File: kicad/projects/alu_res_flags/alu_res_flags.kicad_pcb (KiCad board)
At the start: 2 copper layers, 203.2 x 97.8 mm, 61 parts, among them J1 RES_CRRYBRRW_EQ_IN, J2 Aux_connection, J3 Bus_connection, J4 Control_signal_backplane, J5 ECNZ_OUT, J6 LED_CONTROL, U1 74HC04, U10 74HC245, U11 74HC173, U12 74HC245, U2 74HC377, U3 74HC377, U4 74HC245, U5 74HC245, U6 74HC27, U7 74HC27, U8 74HC30, U9 74HC245

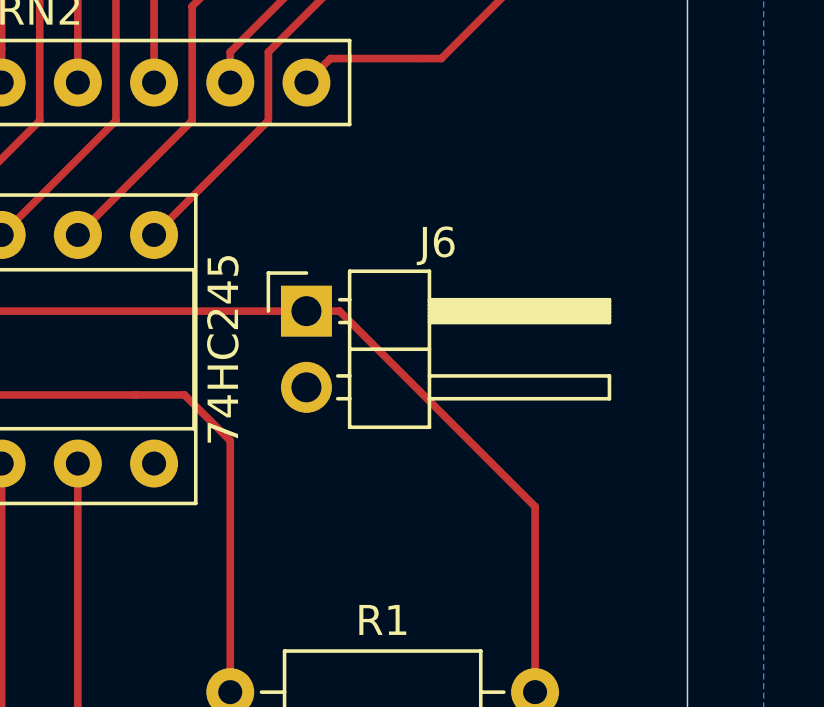
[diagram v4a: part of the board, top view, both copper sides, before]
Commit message: Add better labels to top power and LED control.
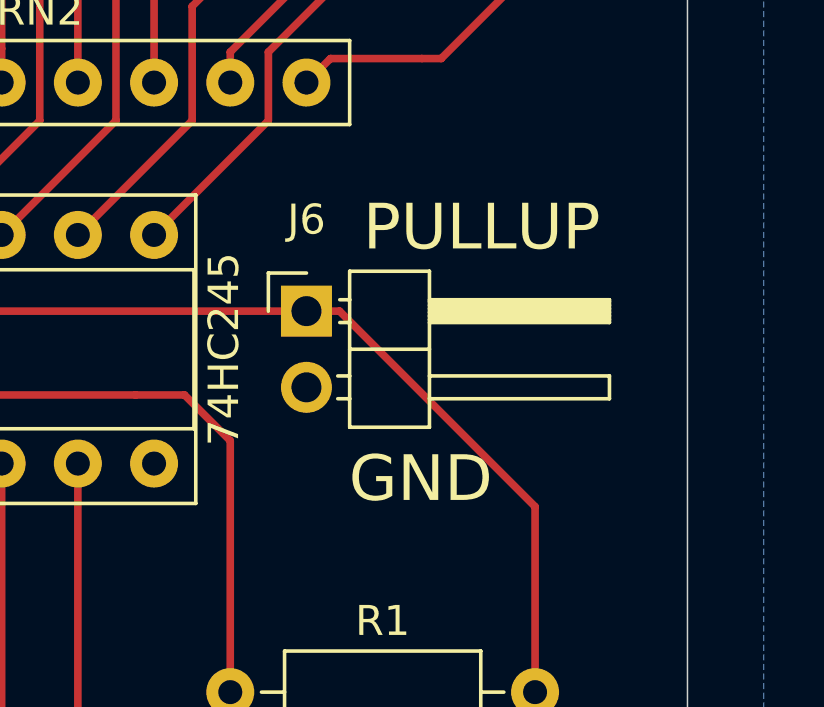
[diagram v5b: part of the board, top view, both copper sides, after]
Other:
- board text added: "GND"
- board text added: "PULLUP"
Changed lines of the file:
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@@
   (general
     (thickness 1.6)
-    (drawings 36)
+    (drawings 38)
     (tracks 1587)
     (zones 0)
@@
   )
   (setup
-    (last_trace_width 0.762)
+    (last_trace_width 0.254)
     (user_trace_width 0.762)
     (trace_clearance 0.2)
@@
     (descr "Through hole angled pin header, 1x02, 2.54mm pitch, 6mm pin length, single row")
     (tags "Through hole angled pin header THT 1x02 2.54mm single row")
-    (fp_text reference J6 (at 4.385 -2.27) (layer F.SilkS)
+    (fp_text reference J6 (at 0 -3.048) (layer F.SilkS)
       (effects (font (size 1 1) (thickness 0.15)))
     )
@@
     )
   )
+  (gr_text GND (at 245.11 89.408) (layer F.SilkS)
+    (effects (font (size 1.524 1.524) (thickness 0.254)))
+  )
+  (gr_text PULLUP (at 247.142 81.026) (layer F.SilkS)
+    (effects (font (size 1.524 1.524) (thickness 0.254)))
+  )
   (gr_arc (start 52.705 151.765) (end 50.8 151.765) (angle -90) (layer Edge.Cuts) (width 0.05))

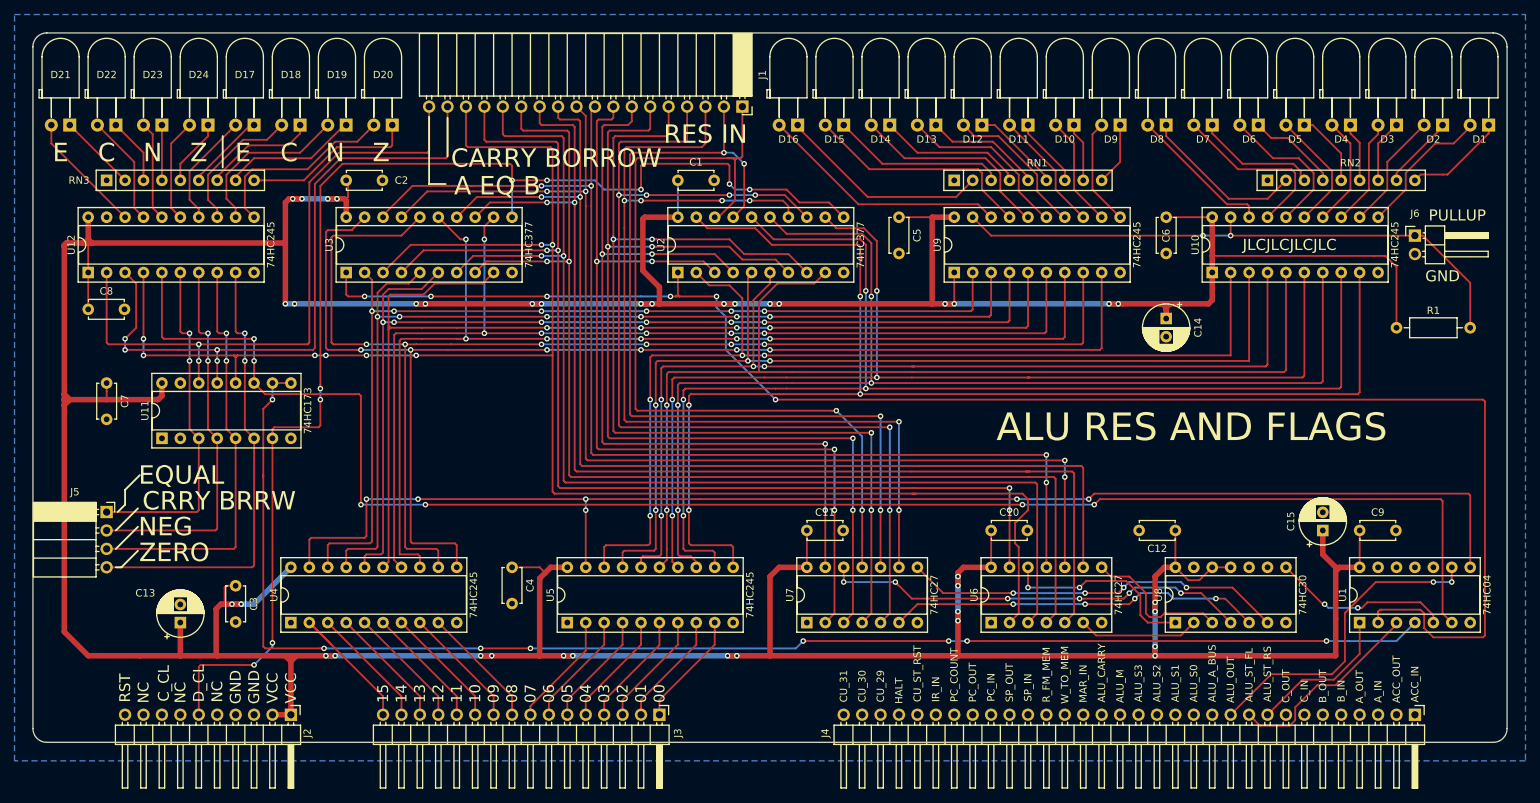
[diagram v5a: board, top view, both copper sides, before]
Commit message: Add pullups on bus output enable and update LED control.
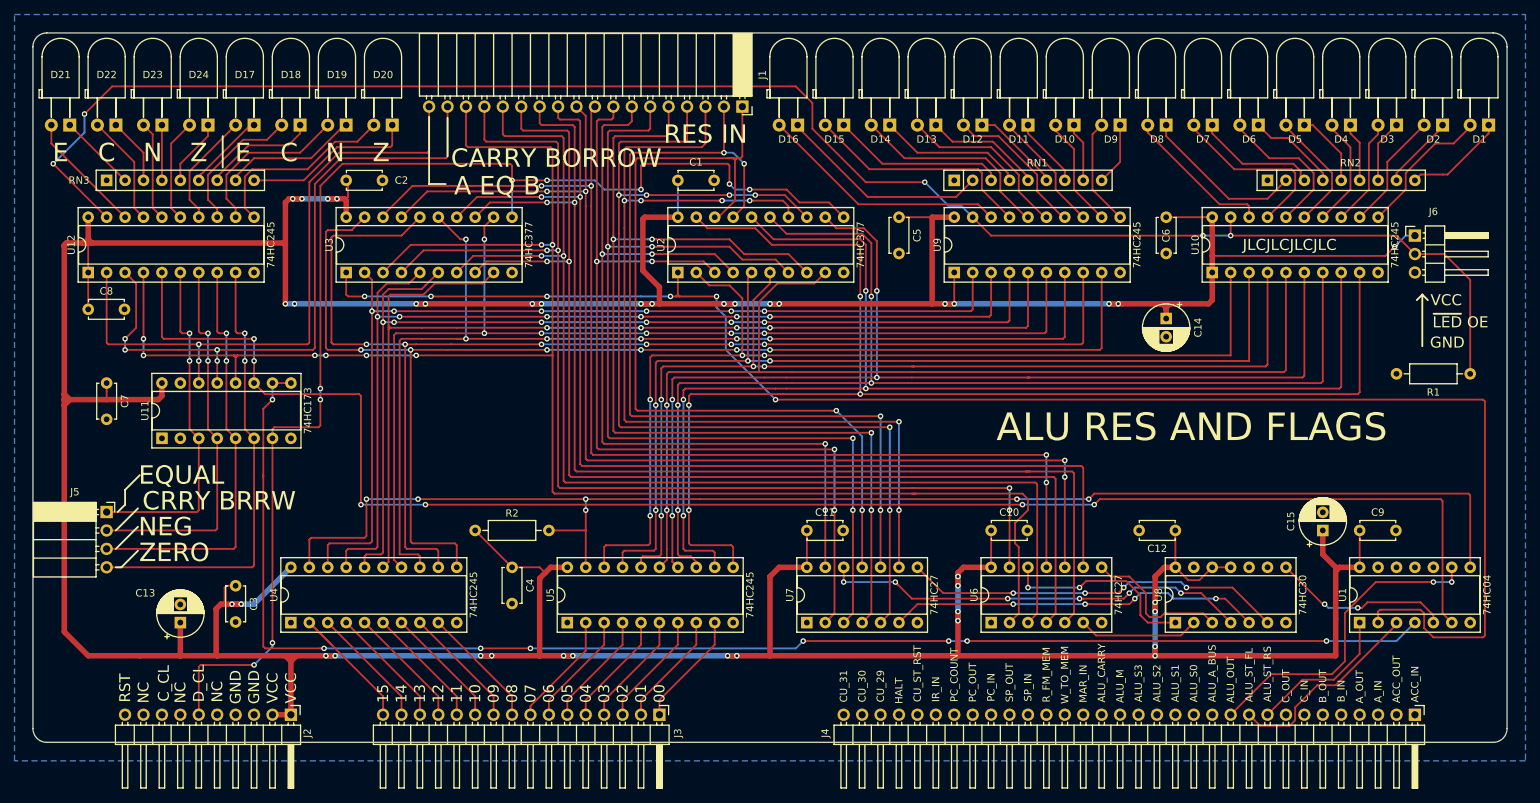
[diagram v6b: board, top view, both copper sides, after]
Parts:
- added R2: 10K, Resistor_THT:R_Axial_DIN0207_L6.3mm_D2.5mm_P10.16mm_Horizontal, F.Cu at (111.8, 124.5)
- J6: footprint Connector_PinHeader_2.54mm:PinHeader_1x02_P2.54mm_Horizontal -> Connector_PinHeader_2.54mm:PinHeader_1x03_P2.54mm_Horizontal
- moved R1 6.35 mm to (238.8, 102.9)
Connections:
- J6 pad 1: /LED_CONTROL -> VCC
- J6 pad 2: GND -> /LED_CONTROL
- R1 pad 1: VCC -> GND
- U12 pad 19: GND -> /LED_CONTROL
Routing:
- net /LED_CONTROL: track 81.1 -> 240.3 mm, vias 2 -> 5
- net /RES_OUT_BAR: track 188.8 -> 193.9 mm
- net VCC: track 736.6 -> 738.5 mm, vias 38 -> 39
- net Net-(D8-Pad2): track 20.1 -> 20.7 mm
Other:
- board text added: "VCC"
- board text added: "~LED OE"
- board text removed: "PULLUP"

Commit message: Tech checks on ALU res flags.
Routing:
- net /CLK_RES_00: track 183.2 -> 173.7 mm
- net /CLK_RES_01: track 172.2 -> 164.5 mm
- net VCC: track 738.5 -> 730.9 mm, vias 39 -> 41
- net /CLK_RES_02: track 165.9 -> 160.4 mm
- net /CLK_RES_07: track 142.3 -> 137.5 mm
- net /CLOCK: track 176.8 -> 172.7 mm
- net /CLK_RES_06: track 139.2 -> 135.2 mm
- net /STORE_FLAGS: track 28.0 -> 31.3 mm
- net /CLK_RES_05: track 140.6 -> 137.4 mm
- net /CLK_RES_03: track 155.3 -> 152.5 mm
- net /RES_OUT: track 44.0 -> 46.8 mm
- net /A_EQ_B: track 89.6 -> 87.0 mm
- net /CARRYBORROW: track 92.1 -> 89.9 mm
- net /CLK_RES_04: track 147.1 -> 144.9 mm
- net Net-(D8-Pad1): track 22.7 -> 20.9 mm
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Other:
- board text added: "CLOCKED"

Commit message: ALU res flags tech checked.
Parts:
- RN1, RN2: value R_Network08_US -> 2K
- RN3: value R_Network08_US -> 10K
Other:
- board text added: "0"
- board text added: "15"
- board text added: "LED ~OE"
- board text added: "NEGATIVE"
- board text added: "V.2"
- board text removed: "CRRY BRRW"
- board text removed: "NEG"
- board text removed: "~LED OE"
